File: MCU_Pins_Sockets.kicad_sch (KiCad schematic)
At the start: 5 parts, among them J1 Conn_01x15_Pin, J2 Conn_01x15_Socket, J3 Conn_01x15_Pin, J4 Conn_01x15_Socket

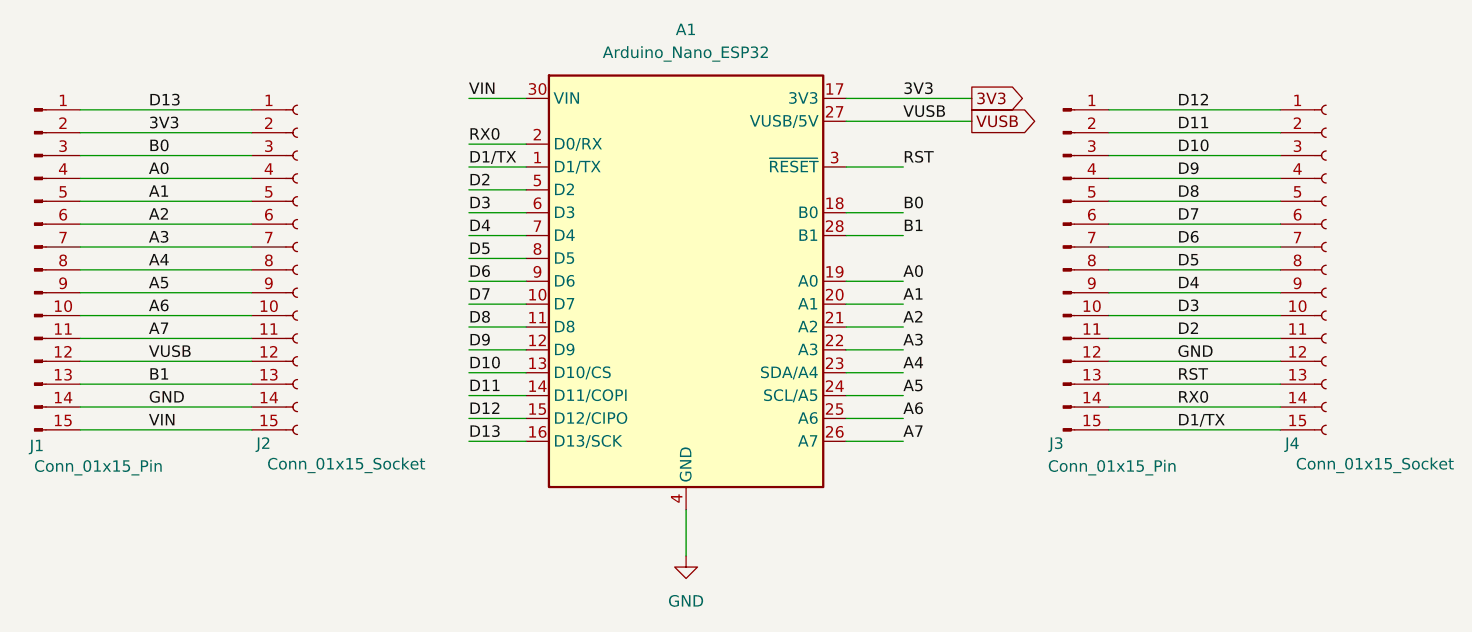
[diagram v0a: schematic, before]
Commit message: - added global nets for A4 and A5
- I2C connetor changes
- Throw swtiches and button identifiers changed

Signed-off-by: deyviaa <legoked@gmail.com>
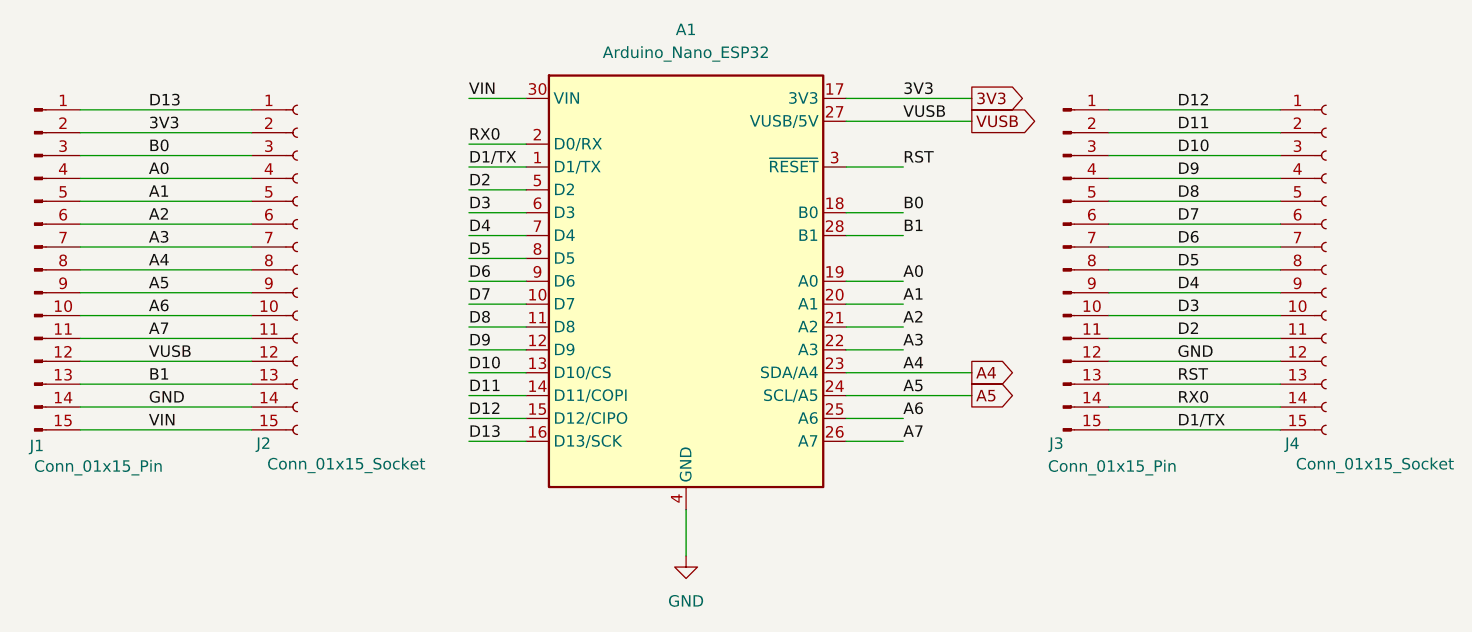
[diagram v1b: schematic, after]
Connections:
- net at A1.18 (B0), A1.19 (A0), A1.30 (VIN)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: no longer A1.23 (SDA/A4), J1.8 (Pin_8), J2.8 (Pin_8)
- new net A4: A1.23 (SDA/A4), J1.8 (Pin_8), J2.8 (Pin_8)
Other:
- title: (none) -> MCU Pinouts
